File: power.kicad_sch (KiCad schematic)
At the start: 76 parts, among them J2 Molex_Mini-Fit_2x3_50362462, Q16 DMG1012T-7, Q2 SISS05DN-T1-GE3, Q23 SISS05DN-T1-GE3, Q24 SISS05DN-T1-GE3, Q25 SISS05DN-T1-GE3, Q39 SISS05DN-T1-GE3, Q4 DMG1012T-7, Q5 SISS05DN-T1-GE3, Q6 DMG1012T-7, Q9 SISS05DN-T1-GE3, U15 NCP718BSN330T1G, U6 LTC4412IS6, U61 LTC4412IS6, U62 LTC4412IS6, U63 LTC4412IS6, U64 LTC4412IS6

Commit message: Update naming on schematic sheets and PCB, update release date
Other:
- title: Jetson AGX Thor Baseboard -> Antmicro Baseboard for Jetson AGX Thor
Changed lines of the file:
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@@
 	(paper "A3")
 	(title_block
-		(title "Jetson AGX Thor Baseboard")
-		(date "2025-11-03")
+		(title "Antmicro Baseboard for Jetson AGX Thor")
+		(date "2026-02-17")
 		(rev "1.1.0")
 		(company "Antmicro Ltd")

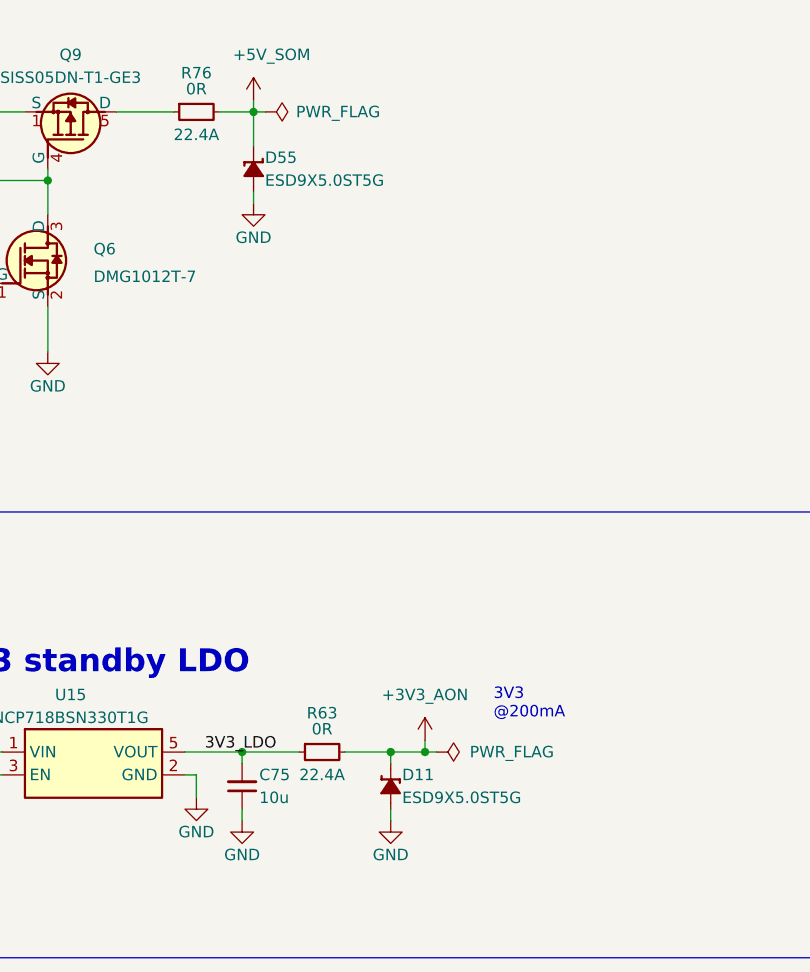
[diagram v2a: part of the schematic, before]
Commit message: [#88664] ESD9X5.0ST5G diodes replaced by PESD5Z5_0F, added TVS on Fan 12V
ESD9X5.0ST5G -> PESD5Z5_0F, changes done on schematics and PCB editor,
added TVS for fan 12V
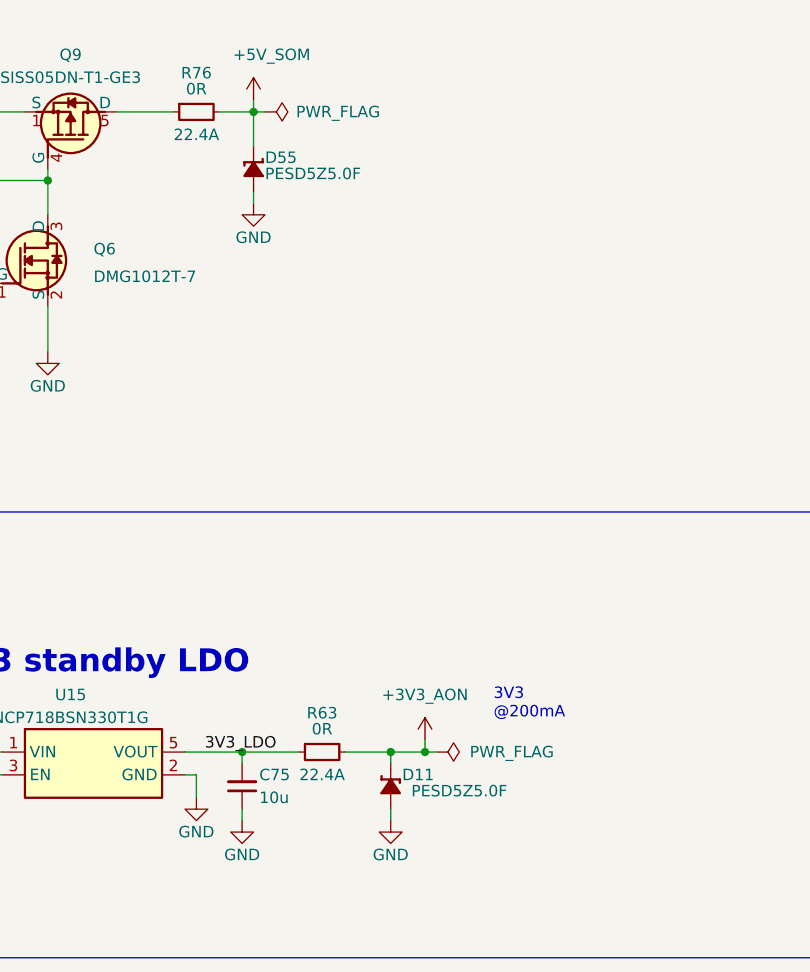
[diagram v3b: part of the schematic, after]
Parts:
- D11, D55: value ESD9X5.0ST5G -> PESD5Z5.0F; footprint antmicro-footprints:SOD-923 -> antmicro-footprints:SOD-523; symbol antmicroTVSDiodes:ESD9X5.0ST5G -> antmicroTVSDiodes:PESD5Z5_0F; MPN ESD9X5.0ST5G -> PESD5Z5.0F; Manufacturer ON Semiconductor -> Nexperia
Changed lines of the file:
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@@
 	)
 	(symbol
-		(lib_id "antmicroTVSDiodes:ESD9X5.0ST5G")
+		(lib_id "antmicroTVSDiodes:PESD5Z5_0F")
 		(at 110.49 62.23 270)
 		(unit 1)
@@
 			)
 		)
-		(property "Value" "ESD9X5.0ST5G"
+		(property "Value" "PESD5Z5.0F"
 			(at 95.25 83.82 0)
 			(effects
@@
 			)
 		)
-		(property "Footprint" "antmicro-footprints:SOD-923"
-			(at 102.87 83.82 0)
+		(property "Footprint" "antmicro-footprints:SOD-523"
+			(at 105.41 77.47 0)
 			(effects
 				(font
@@
 			)
 		)
-		(property "Datasheet" "https://www.onsemi.com/pdf/datasheet/esd9x3.3st5g-d.pdf"
-			(at 100.33 83.82 0)
+		(property "Datasheet" "https://assets.nexperia.com/documents/data-sheet/PESD5Z5_0.pdf"
+			(at 102.87 77.47 0)
 			(effects
 				(font
@@
 			)
 		)
-		(property "Description" "Unidirectional TVS, 30 kV,  SOD-923, 5 V, 65 pF"
-			(at 110.49 62.23 0)
+		(property "Description" "Unidirectional TVS, 30 kV,  SOD-523, 5 V, 89 pF"
+			(at 90.17 77.47 0)
 			(effects
 				(font
 					(size 1.27 1.27)
 				)
+				(justify left bottom)
 				(hide yes)
 			)
 		)
-		(property "Manufacturer" "ON Semiconductor"
-			(at 97.79 83.82 0)
+		(property "Manufacturer" "Nexperia"
+			(at 100.33 77.47 0)
 			(effects
 				(font
@@
 			)
 		)
-		(property "MPN" "ESD9X5.0ST5G"
+		(property "MPN" "PESD5Z5.0F"
 			(at 111.76 66.04 90)
 			(effects
@@
 					(thickness 0.15)
 				)
-				(justify left)
+				(justify left bottom)
 			)
 		)
 		(property "Author" "Antmicro"
-			(at 92.71 83.82 0)
+			(at 95.25 77.47 0)
 			(effects
 				(font
@@
 		)
 		(property "License" "Apache-2.0"
-			(at 90.17 83.82 0)
+			(at 92.71 77.47 0)
 			(effects
 				(font
@@
 	)
 	(symbol
-		(lib_id "antmicroTVSDiodes:ESD9X5.0ST5G")
+		(lib_id "antmicroTVSDiodes:PESD5Z5_0F")
 		(at 125.73 130.81 90)
 		(mirror x)
@@
 			)
 		)
-		(property "Value" "ESD9X5.0ST5G"
+		(property "Value" "PESD5Z5.0F"
 			(at 140.97 152.4 0)
 			(effects
@@
 			)
 		)
-		(property "Footprint" "antmicro-footprints:SOD-923"
-			(at 133.35 152.4 0)
+		(property "Footprint" "antmicro-footprints:SOD-523"
+			(at 130.81 146.05 0)
 			(effects
 				(font
@@
 			)
 		)
-		(property "Datasheet" "https://www.onsemi.com/pdf/datasheet/esd9x3.3st5g-d.pdf"
-			(at 135.89 152.4 0)
+		(property "Datasheet" "https://assets.nexperia.com/documents/data-sheet/PESD5Z5_0.pdf"
+			(at 133.35 146.05 0)
 			(effects
 				(font
@@
 			)
 		)
-		(property "Description" "Unidirectional TVS, 30 kV,  SOD-923, 5 V, 65 pF"
-			(at 125.73 130.81 0)
+		(property "Description" "Unidirectional TVS, 30 kV,  SOD-523, 5 V, 89 pF"
+			(at 146.05 146.05 0)
 			(effects
 				(font
 					(size 1.27 1.27)
 				)
+				(justify left bottom)
 				(hide yes)
 			)
 		)
-		(property "Manufacturer" "ON Semiconductor"
-			(at 138.43 152.4 0)
+		(property "Manufacturer" "Nexperia"
+			(at 135.89 146.05 0)
 			(effects
 				(font
@@
 			)
 		)
-		(property "MPN" "ESD9X5.0ST5G"
-			(at 127 134.62 90)
+		(property "MPN" "PESD5Z5.0F"
+			(at 138.684 134.62 90)
 			(effects
 				(font
@@
 					(thickness 0.15)
 				)
-				(justify right)
+				(justify left bottom)
 			)
 		)
 		(property "Author" "Antmicro"
-			(at 143.51 152.4 0)
+			(at 140.97 146.05 0)
 			(effects
 				(font
@@
 		)
 		(property "License" "Apache-2.0"
-			(at 146.05 152.4 0)
+			(at 143.51 146.05 0)
 			(effects
 				(font

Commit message: [#89204] Power selector with MAX16013
Added over-voltage protection using MAX16013 IC, also reverse-voltage
protection was redesigned using the same IC MAX16013 as in OVP
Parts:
- removed C30: C_100n_0402, antmicro-footprints:C_0402_1005Metric, symbol antmicroCapacitors0402:C_100n_0402
- removed C34: C_1u_25V_0402, antmicro-footprints:C_0402_1005Metric, symbol antmicroCapacitors0402:C_1u_25V_0402
- removed Q2, Q39: SISS05DN-T1-GE3, antmicro-footprints:Vishay_PowerPAK_1212-8_Single, symbol antmicroTransistorsFETsMOSFETsSingle:SISS05DN-T1-GE3
- removed U6: LTC4412IS6, antmicro-footprints:SOT-23-6, symbol antmicroPMICORControllersIdealDiodes:LTC4412IS6
- added C357: C_100n_0402, antmicro-footprints:C_0402_1005Metric, symbol antmicroCapacitors0402:C_100n_0402
- added Q32, Q33, Q41, Q42: SISS05DN-T1-GE3, antmicro-footprints:Vishay_PowerPAK_1212-8_Single, symbol antmicroTransistorsFETsMOSFETsSingle:SISS05DN-T1-GE3
- added R409: R_232k_0402, antmicro-footprints:R_0402_1005Metric, symbol antmicroResistors0402:R_232k_0402
- added R411: R_11k8_0402, antmicro-footprints:R_0402_1005Metric, symbol antmicroResistors0402:R_11k8_0402
- added R412: R_10k_0402, antmicro-footprints:R_0402_1005Metric, symbol antmicroResistors0402:R_10k_0402
- added TP116: TP_0.75mm_SMD, antmicro-footprints:TP_SMD_0.75mm, symbol antmicroTestPoints:TP_0.75mm_SMD
- added U9: MAX16013, antmicro-footprints:TDFN-6-1EP_3x3mm_P0.95, symbol antmicroOverUnderVoltageProtection:MAX16013
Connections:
- net GND: now also C357.1, R411.1, U9.2 (GND)
- net VCC: now also Q41.5 (D), Q42.5 (D)
- net VCC_IN: now also Q32.5 (D), Q33.5 (D)
- new net: Q41.4 (G), Q42.4 (G), U9.3 (GATE2)
- new net: R412.1, TP116.1, U9.5 (EN)
- new net: R409.1, R411.2, U9.4 (SET)
- new net: Q32.4 (G), Q33.4 (G), U9.6 (GATE1)
- new net VCC_NO_OVP: C357.2, Q32.1 (S), Q32.2 (S), Q32.3 (S), Q33.1 (S), Q33.2 (S), Q33.3 (S), Q41.1 (S), Q41.2 (S), Q41.3 (S), Q42.1 (S), Q42.2 (S), Q42.3 (S), R409.2, R412.2, U9.1 (VCC)
- no-connect marks 5 -> 4
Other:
- note removed: "Ideal-diode O-Ring"
- moved on the sheet: C236, C240, C261, C262, C263, C264, C265, C266, C38, D2, J2, Q23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

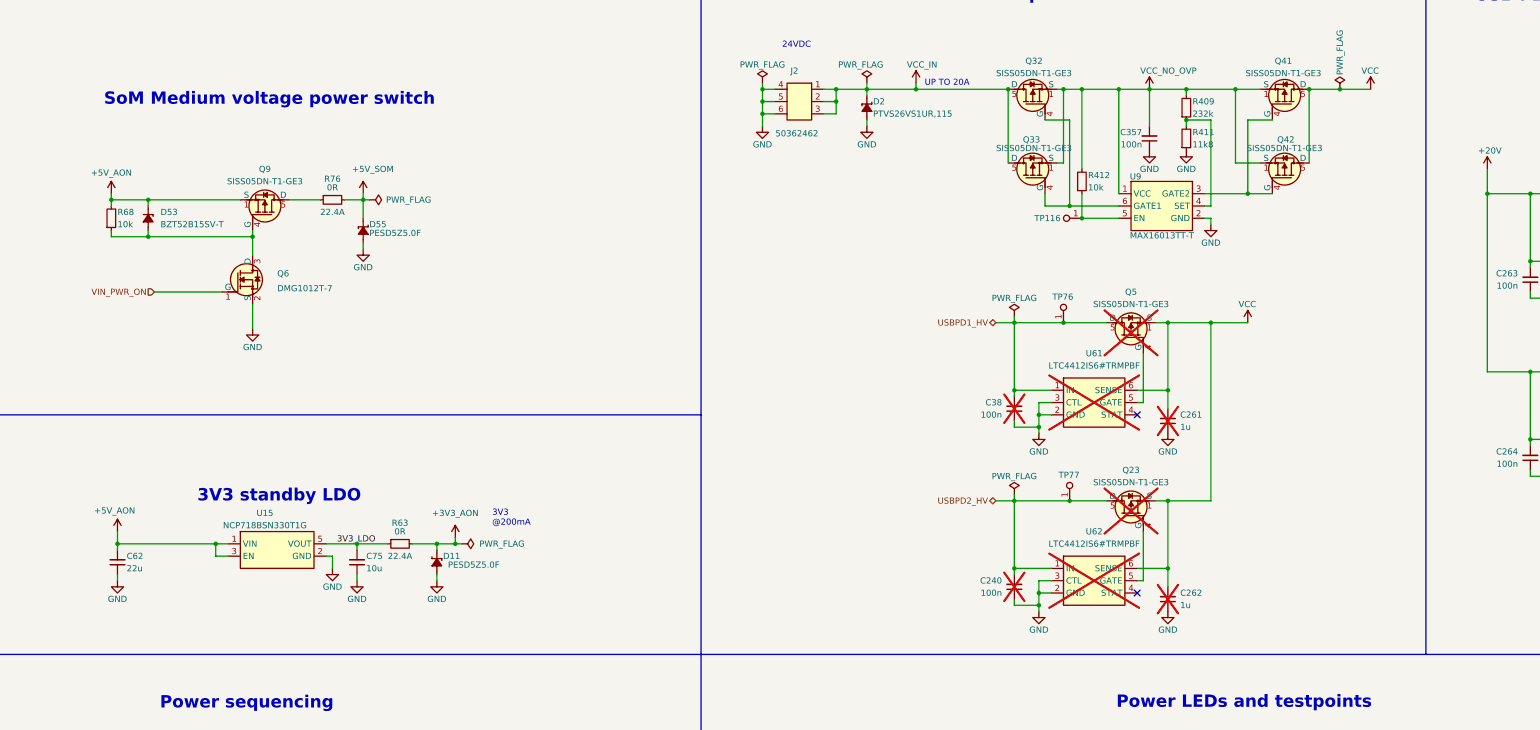
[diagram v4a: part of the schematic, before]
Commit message: [#89142] Proposal of Latch circuit for OVP
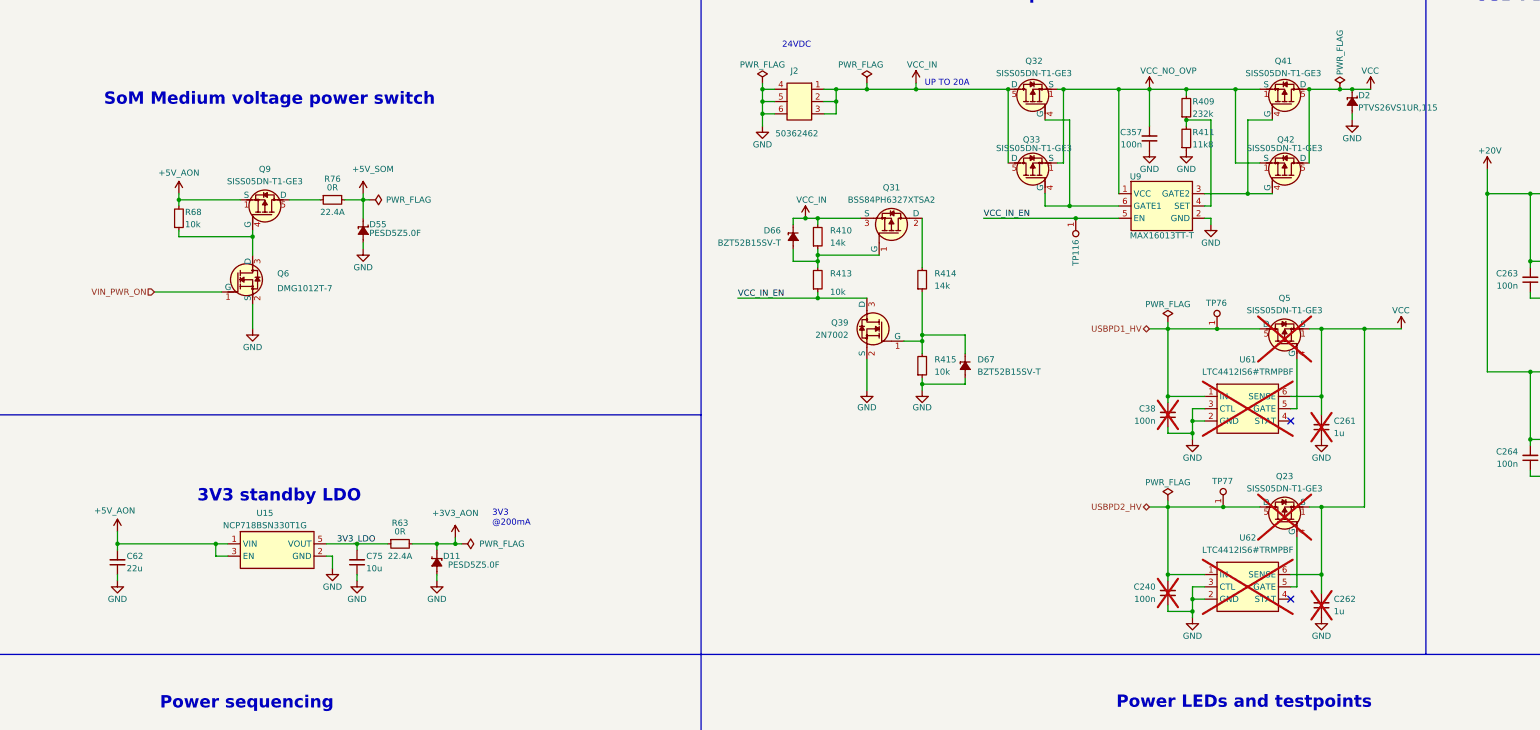
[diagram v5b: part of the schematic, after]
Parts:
- removed D53: BZT52B15SV-T, antmicro-footprints:D_SOD-323, symbol antmicroDiodesZenerSingle:BZT52B15SV-T
- removed R412: R_10k_0402, antmicro-footprints:R_0402_1005Metric, symbol antmicroResistors0402:R_10k_0402
- added D66, D67: BZT52B15SV-T, antmicro-footprints:D_SOD-323, symbol antmicroDiodesZenerSingle:BZT52B15SV-T
- added Q31: BSS84PH6327XTSA2, antmicro-footprints:SOT-23-3, symbol antmicroTransistorsFETsMOSFETsSingle:BSS84PH6327XTSA2
- added Q39: 2N7002_SOT-23-3, antmicro-footprints:SOT-23-3, symbol antmicroTransistorsFETsMOSFETsSingle:2N7002_SOT-23-3
- added R410, R414: R_14k_0402, antmicro-footprints:R_0402_1005Metric, symbol antmicroResistors0402:R_14k_0402
- added R413, R415: R_10k_0402, antmicro-footprints:R_0402_1005Metric, symbol antmicroResistors0402:R_10k_0402
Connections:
- net GND: now also D67.2 (A), Q39.2 (S), R415.1
- net VCC: now also D2.1 (C)
- net VCC_IN: now also D66.1 (C), Q31.3 (S), R410.2; no longer D2.1 (C)
- net VCC_IN_EN: now reaches TP116.1, U9.5 (EN)
- net VCC_IN_EN: now also Q39.3 (D), R413.1
- new net: D67.1 (C), Q39.1 (G), R414.1, R415.2
- new net: Q31.2 (D), R414.2
- new net: D66.2 (A), Q31.1 (G), R410.1, R413.2
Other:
- moved on the sheet: C240, C261, C262, C38, D2, Q23, Q5, R68, TP116, TP76, TP77, U61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

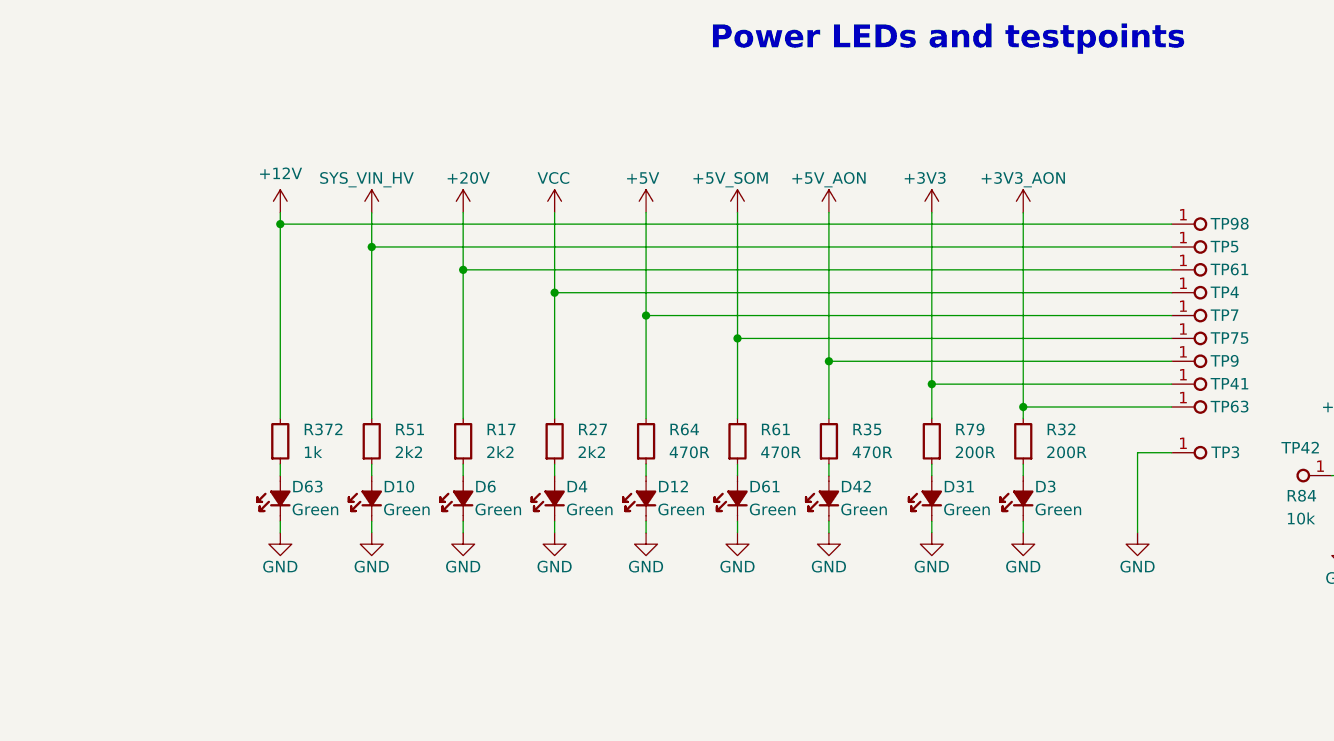
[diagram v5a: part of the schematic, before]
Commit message: [#89536] Add redundant VCC LED
Used for front panel Power LED
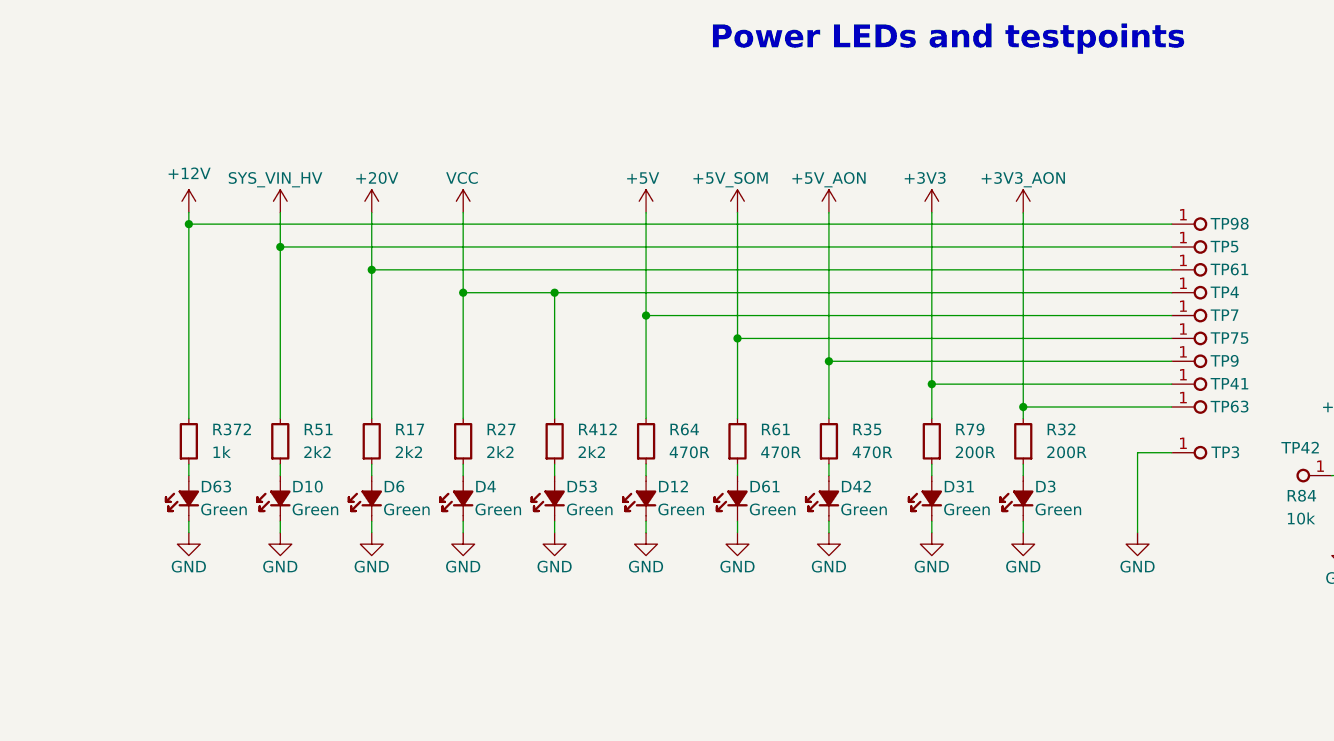
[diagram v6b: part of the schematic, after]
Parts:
- added D53: LED_G_0603_LTST-C190GKT, antmicro-footprints:LED_0603_1608Metric_G, symbol antmicroLEDIndicationDiscrete:LED_G_0603_LTST-C190GKT
- added R412: R_2k2_0402, antmicro-footprints:R_0402_1005Metric, symbol antmicroResistors0402:R_2k2_0402
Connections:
- net GND: now also D53.1 (C)
- net VCC: now also R412.2
- new net: D53.2 (A), R412.1
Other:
- moved on the sheet: D10, D4, D6, D63, R17, R27, R372, R51
